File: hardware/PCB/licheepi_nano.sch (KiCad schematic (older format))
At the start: 4 parts

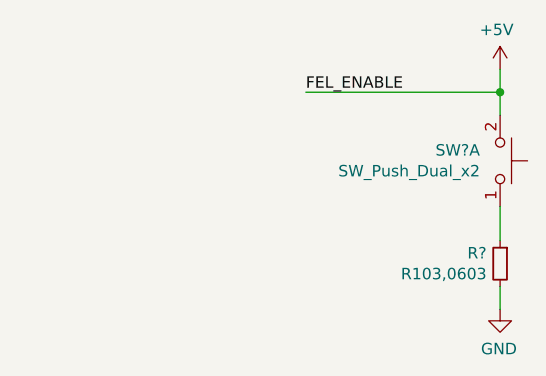
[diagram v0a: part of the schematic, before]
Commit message: update for adding usb ttl converter,
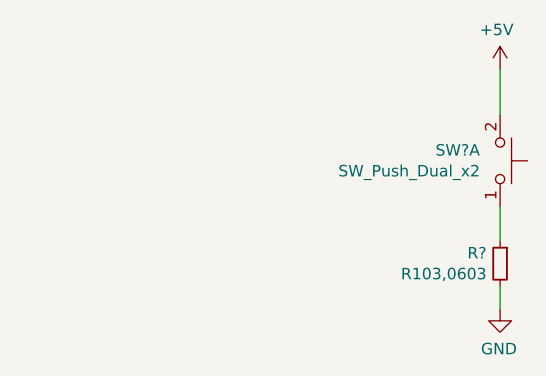
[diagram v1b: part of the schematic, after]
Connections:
- net +5V: no longer U?.58 (SPI0-CLK)
- new net FEL_ENABLE: U?.58 (SPI0-CLK)
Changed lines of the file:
@@
 Wire Wire Line
 	10850 1450 10850 1600
-Wire Wire Line
-	10850 850  10850 950
 $Comp
 L customized_power:+5V #PWR?
@@
 	0    1    -1   0
 $EndComp
-Text Label 10000 950  0    50   ~ 0
-FEL_ENABLE
-Wire Wire Line
-	10000 950  10850 950
-Connection ~ 10850 950
-Wire Wire Line
-	10850 950  10850 1050
 Text Label 9750 3250 2    50   ~ 0
 FEL_ENABLE
@@
 Wire Wire Line
 	5300 5700 5300 6250
+Wire Wire Line
+	10850 850  10850 1050
 $EndSCHEMATC

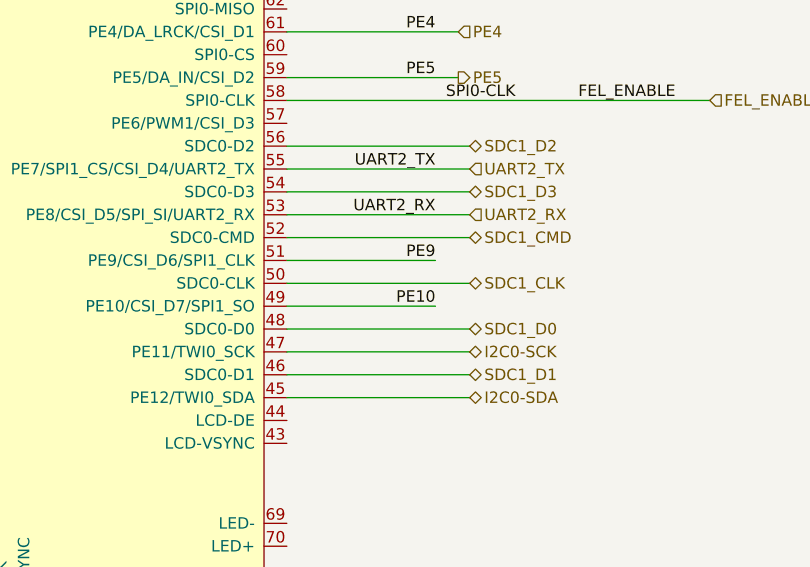
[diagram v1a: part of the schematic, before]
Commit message: sch: update buzzer connection,
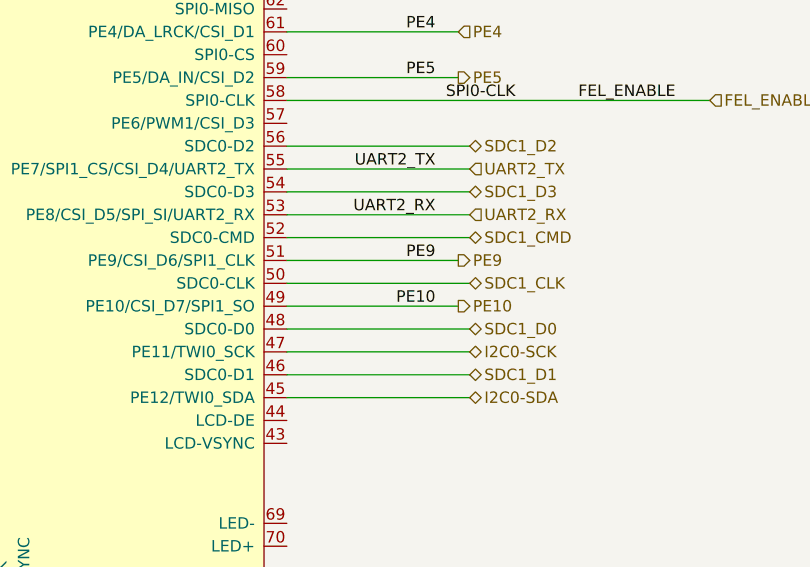
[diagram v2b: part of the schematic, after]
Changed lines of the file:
@@
 Text Label 8700 4150 2    50   ~ 0
 PE10
-Wire Wire Line
-	8050 4150 8700 4150
 Text Label 8700 3950 2    50   ~ 0
 PE9
-Wire Wire Line
-	8050 3950 8700 3950
 Text Label 8700 3150 2    50   ~ 0
 PE5
@@
 Wire Wire Line
 	10850 850  10850 1050
+Text HLabel 8800 3950 2    50   Output ~ 0
+PE9
+Text HLabel 8800 4150 2    50   Output ~ 0
+PE10
+Wire Wire Line
+	8050 3950 8800 3950
+Wire Wire Line
+	8050 4150 8800 4150
 $EndSCHEMATC

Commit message: update for io_bank,
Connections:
- net USB_DM: now reaches U?.1 (USB_DM)
- net +3V3: now reaches U?.12 (3V3)
- net PA0: now reaches U?.14 (PA0)
- net PA1: now reaches U?.16 (PA1)
- net USB_DP: now reaches U?.3 (USB_DP)
- net PE6: now reaches U?.57 (PE6/PWM1/CSI_D3)
- net UART1_RX renamed PA2
- net UART1_TX renamed PA3
- net UART2_RX renamed PE8
- net UART2_TX renamed PE7
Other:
- moved on the sheet: C?, U?

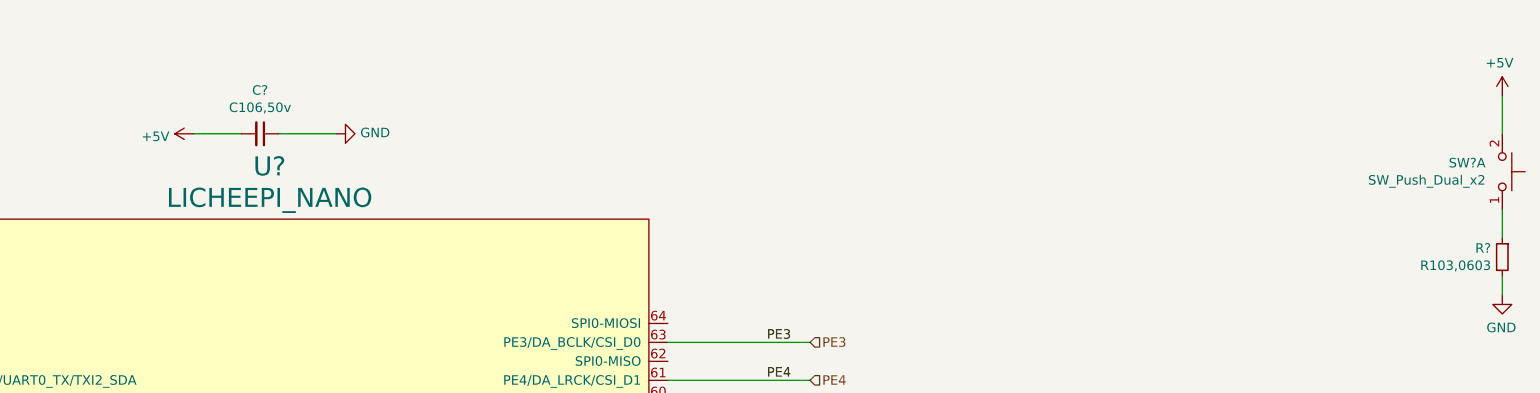
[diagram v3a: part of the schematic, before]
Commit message: update rtl8723 circuit,
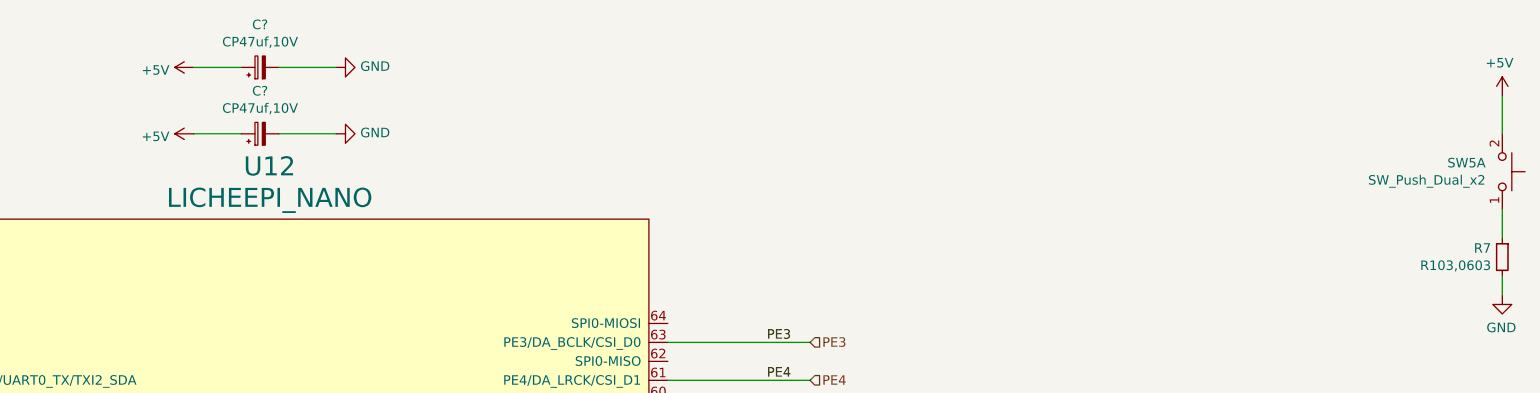
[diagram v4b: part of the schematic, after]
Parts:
- removed C?: C106,50v, symbol taobao-c:C106,50v
- added C? (x2): CP47uf,10V, Capacitor_SMD:CP_Elec_4x5.3, symbol taobao-cp:CP47uf,10V
- SW5: renamed from SW?; footprint (none) -> footprint-lib:SW_SPST_PTS645
- U12: renamed from U?; footprint (none) -> footprint-lib:licheepi_nano
- gave numbers to parts that had none: 1
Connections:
- net +5V: now also C?.1, C?.1
- net GND: now also C?.2, C?.2
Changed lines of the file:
@@
 $EndDescr
 $Comp
-L taobao-components:LICHEEPI_NANO U?
+L taobao-components:LICHEEPI_NANO U12
 U 1 1 5E87B06D
 P 4350 3500
-F 0 "U?" H 4350 5777 100 0000 C CNN
+F 0 "U12" H 4350 5777 100 0000 C CNN
 F 1 "LICHEEPI_NANO" H 4350 5611 100 0000 C CNN
-F 2 "" H 4400 3700 50  0001 C CNN
+F 2 "footprint-lib:licheepi_nano" H 4400 3700 50  0001 C CNN
 F 3 "" H 4400 3700 50  0001 C CNN
 	1    4350 3500
@@
 $EndComp
 $Comp
-L taobao-r:R103,0603 R?
+L taobao-r:R103,0603 R7
 U 1 1 5E88E564
 P 10850 1700
-F 0 "R?" H 10909 1746 50  0000 L CNN
+F 0 "R7" H 10909 1746 50  0000 L CNN
 F 1 "R103,0603" H 10909 1655 50  0000 L CNN
 F 2 "Resistor_SMD:R_0603_1608Metric_Pad1.05x0.95mm_HandSolder" H 10850 1700 50  0001 C CNN
@@
 $EndComp
 $Comp
-L Switch:SW_Push_Dual_x2 SW?
+L Switch:SW_Push_Dual_x2 SW5
 U 1 1 5E88E56A
 P 10850 1250
-F 0 "SW?" V 10896 1162 50  0000 R CNN
+F 0 "SW5" V 10896 1162 50  0000 R CNN
 F 1 "SW_Push_Dual_x2" V 10805 1162 50  0000 R CNN
-F 2 "" H 10850 1450 50  0001 C CNN
+F 2 "footprint-lib:SW_SPST_PTS645" H 10850 1450 50  0001 C CNN
 F 3 "~" H 10850 1450 50  0001 C CNN
 	1    10850 1250
@@
 $EndComp
 $Comp
-L taobao-c:C106,50v C?
-U 1 1 5E8969B5
-P 4300 1050
-F 0 "C?" V 4071 1050 50  0000 C CNN
-F 1 "C106,50v" V 4162 1050 50  0000 C CNN
-F 2 "" H 4300 1050 50  0001 C CNN
-F 3 "~" H 4300 1050 50  0001 C CNN
-	1    4300 1050
-	0    1    1    0
-$EndComp
-$Comp
 L power:GND #PWR0106
 U 1 1 5E896ED8
@@
 PA3
 $Comp
-L customized_power:+3V3 #PWR?
+L customized_power:+3V3 #PWR0136
 U 1 1 5EB508F7
 P 1350 3150
-F 0 "#PWR?" H 1350 3000 50  0001 C CNN
+F 0 "#PWR0136" H 1350 3000 50  0001 C CNN
 F 1 "+3V3" V 1365 3278 50  0000 L CNN
 F 2 "" H 1350 3150 50  0001 C CNN
@@
 Wire Wire Line
 	1850 2250 2250 2250
+$Comp
+L taobao-cp:CP47uf,10V C?
+U 1 1 5EA532C5
+P 4300 1050
+F 0 "C?" V 4525 1050 50  0000 C CNN
+F 1 "CP47uf,10V" V 4434 1050 50  0000 C CNN
+F 2 "Capacitor_SMD:CP_Elec_4x5.3" H 4300 1050 50  0001 C CNN
+F 3 "~" H 4300 1050 50  0001 C CNN
+	1    4300 1050
+	0    -1   -1   0
+$EndComp
+$Comp
+L customized_power:+5V #PWR?
+U 1 1 5EA55272
+P 3950 700
+AR Path="/5E87CEF1/5EA55272" Ref="#PWR?"  Part="1"
+AR Path="/5E87A116/5EA55272" Ref="#PWR?"  Part="1"
+F 0 "#PWR?" H 3950 550 50  0001 C CNN
+F 1 "+5V" V 3965 828 50  0000 L CNN
+F 2 "" H 3950 700 50  0001 C CNN
+F 3 "" H 3950 700 50  0001 C CNN
+	1    3950 700
+	0    -1   1    0
+$EndComp
+$Comp
+L power:GND #PWR?
+U 1 1 5EA5527C
+P 4700 700
+F 0 "#PWR?" H 4700 450 50  0001 C CNN
+F 1 "GND" V 4705 572 50  0000 R CNN
+F 2 "" H 4700 700 50  0001 C CNN
+F 3 "" H 4700 700 50  0001 C CNN
+	1    4700 700
+	0    -1   -1   0
+$EndComp
+Wire Wire Line
+	3950 700  4200 700
+Wire Wire Line
+	4400 700  4700 700
+$Comp
+L taobao-cp:CP47uf,10V C?
+U 1 1 5EA55288
+P 4300 700
+F 0 "C?" V 4525 700 50  0000 C CNN
+F 1 "CP47uf,10V" V 4434 700 50  0000 C CNN
+F 2 "Capacitor_SMD:CP_Elec_4x5.3" H 4300 700 50  0001 C CNN
+F 3 "~" H 4300 700 50  0001 C CNN
+	1    4300 700
+	0    -1   -1   0
+$EndComp
 $EndSCHEMATC

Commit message: update,
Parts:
- SW5: value SW_Push_Dual_x2 -> RESET
- gave numbers to parts that had none: 2
- renumbered U12 to U2
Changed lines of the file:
@@
 $Descr A4 11693 8268
 encoding utf-8
-Sheet 6 6
+Sheet 5 6
 Title ""
 Date ""
@@
 $EndDescr
 $Comp
-L taobao-components:LICHEEPI_NANO U12
+L taobao-components:LICHEEPI_NANO U2
 U 1 1 5E87B06D
 P 4350 3500
-F 0 "U12" H 4350 5777 100 0000 C CNN
+F 0 "U2" H 4350 5777 100 0000 C CNN
 F 1 "LICHEEPI_NANO" H 4350 5611 100 0000 C CNN
 F 2 "footprint-lib:licheepi_nano" H 4400 3700 50  0001 C CNN
@@
 P 10850 850
 AR Path="/5E87CEF1/5E88E558" Ref="#PWR?"  Part="1"
-AR Path="/5E87A116/5E88E558" Ref="#PWR0103"  Part="1"
-F 0 "#PWR0103" H 10850 700 50  0001 C CNN
+AR Path="/5E87A116/5E88E558" Ref="#PWR024"  Part="1"
+F 0 "#PWR024" H 10850 700 50  0001 C CNN
 F 1 "+5V" H 10865 1023 50  0000 C CNN
 F 2 "" H 10850 850 50  0001 C CNN
@@
 $EndComp
 $Comp
-L power:GND #PWR0104
+L power:GND #PWR025
 U 1 1 5E88E55E
 P 10850 1900
-F 0 "#PWR0104" H 10850 1650 50  0001 C CNN
+F 0 "#PWR025" H 10850 1650 50  0001 C CNN
 F 1 "GND" H 10855 1727 50  0000 C CNN
 F 2 "" H 10850 1900 50  0001 C CNN
@@
 P 10850 1250
 F 0 "SW5" V 10896 1162 50  0000 R CNN
-F 1 "SW_Push_Dual_x2" V 10805 1162 50  0000 R CNN
+F 1 "RESET" V 10805 1162 50  0000 R CNN
 F 2 "footprint-lib:SW_SPST_PTS645" H 10850 1450 50  0001 C CNN
 F 3 "~" H 10850 1450 50  0001 C CNN
@@
 P 3950 1050
 AR Path="/5E87CEF1/5E895245" Ref="#PWR?"  Part="1"
-AR Path="/5E87A116/5E895245" Ref="#PWR0105"  Part="1"
-F 0 "#PWR0105" H 3950 900 50  0001 C CNN
+AR Path="/5E87A116/5E895245" Ref="#PWR021"  Part="1"
+F 0 "#PWR021" H 3950 900 50  0001 C CNN
 F 1 "+5V" V 3965 1178 50  0000 L CNN
 F 2 "" H 3950 1050 50  0001 C CNN
@@
 $EndComp
 $Comp
-L power:GND #PWR0106
+L power:GND #PWR023
 U 1 1 5E896ED8
 P 4700 1050
-F 0 "#PWR0106" H 4700 800 50  0001 C CNN
+F 0 "#PWR023" H 4700 800 50  0001 C CNN
 F 1 "GND" V 4705 922 50  0000 R CNN
 F 2 "" H 4700 1050 50  0001 C CNN
@@
 P 1350 2750
 AR Path="/5E87CEF1/5E89C8DE" Ref="#PWR?"  Part="1"
-AR Path="/5E87A116/5E89C8DE" Ref="#PWR0107"  Part="1"
-F 0 "#PWR0107" H 1350 2600 50  0001 C CNN
+AR Path="/5E87A116/5E89C8DE" Ref="#PWR017"  Part="1"
+F 0 "#PWR017" H 1350 2600 50  0001 C CNN
 F 1 "+5V" V 1365 2878 50  0000 L CNN
 F 2 "" H 1350 2750 50  0001 C CNN
@@
 	1350 2750 2250 2750
 $Comp
-L power:GND #PWR0108
+L power:GND #PWR018
 U 1 1 5E89D911
 P 1350 2950
-F 0 "#PWR0108" H 1350 2700 50  0001 C CNN
+F 0 "#PWR018" H 1350 2700 50  0001 C CNN
 F 1 "GND" V 1355 2822 50  0000 R CNN
 F 2 "" H 1350 2950 50  0001 C CNN
@@
 PA3
 $Comp
-L customized_power:+3V3 #PWR0136
+L customized_power:+3V3 #PWR019
 U 1 1 5EB508F7
 P 1350 3150
-F 0 "#PWR0136" H 1350 3000 50  0001 C CNN
+F 0 "#PWR019" H 1350 3000 50  0001 C CNN
 F 1 "+3V3" V 1365 3278 50  0000 L CNN
 F 2 "" H 1350 3150 50  0001 C CNN
@@
 	1850 2250 2250 2250
 $Comp
-L taobao-cp:CP47uf,10V C?
+L taobao-cp:CP47uf,10V C2
 U 1 1 5EA532C5
 P 4300 1050
-F 0 "C?" V 4525 1050 50  0000 C CNN
+F 0 "C2" V 4525 1050 50  0000 C CNN
 F 1 "CP47uf,10V" V 4434 1050 50  0000 C CNN
 F 2 "Capacitor_SMD:CP_Elec_4x5.3" H 4300 1050 50  0001 C CNN
@@
 P 3950 700
 AR Path="/5E87CEF1/5EA55272" Ref="#PWR?"  Part="1"
-AR Path="/5E87A116/5EA55272" Ref="#PWR?"  Part="1"
-F 0 "#PWR?" H 3950 550 50  0001 C CNN
+AR Path="/5E87A116/5EA55272" Ref="#PWR020"  Part="1"
+F 0 "#PWR020" H 3950 550 50  0001 C CNN
 F 1 "+5V" V 3965 828 50  0000 L CNN
 F 2 "" H 3950 700 50  0001 C CNN
@@
 $EndComp
 $Comp
-L power:GND #PWR?
+L power:GND #PWR022
 U 1 1 5EA5527C
 P 4700 700
-F 0 "#PWR?" H 4700 450 50  0001 C CNN
+F 0 "#PWR022" H 4700 450 50  0001 C CNN
 F 1 "GND" V 4705 572 50  0000 R CNN
 F 2 "" H 4700 700 50  0001 C CNN
@@
 	4400 700  4700 700
 $Comp
-L taobao-cp:CP47uf,10V C?
+L taobao-cp:CP47uf,10V C1
 U 1 1 5EA55288
 P 4300 700
-F 0 "C?" V 4525 700 50  0000 C CNN
+F 0 "C1" V 4525 700 50  0000 C CNN
 F 1 "CP47uf,10V" V 4434 700 50  0000 C CNN
 F 2 "Capacitor_SMD:CP_Elec_4x5.3" H 4300 700 50  0001 C CNN
